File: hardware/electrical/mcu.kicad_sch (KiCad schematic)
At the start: 0 parts

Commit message: Add microcontroller and pinout to schematic
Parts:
- added C? (x2): 2u2, symbol Device:C_Small
- added C? (x14): 100n, symbol Device:C_Small
- added C?: 4u7, symbol Device:C_Small
- added C? (x2): 1u, symbol Device:C_Small
- added U?: STM32F446ZETx, Package_QFP:LQFP-144_20x20mm_P0.5mm, symbol MCU_ST_STM32F4:STM32F446ZETx
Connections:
- new net: C?.1, U?.71 (VCAP_1)
- new net: C?.1, U?.106 (VCAP_2)
- new net +3V3: C?.1, C?.1, C?.1, C?.1, C?.1, C?.1, C?.1, C?.1, C?.1, C?.1, C?.1, C?.1, C?.1, C?.1, C?.1, C?.1, C?.1, U?.108 (VDD), U?.121 (VDD), U?.131 (VDD), U?.144 (VDD), U?.17 (VDD), U?.30 (VDD), U?.32 (VREF+), U?.33 (VDDA), U?.39 (VDD), U?.52 (VDD), U?.62 (VDD), U?.72 (VDD), U?.84 (VDD), U?.95 (VDDUSB)
- new net BOOT0: U?.138 (BOOT0)
- new net DCMI_D0: U?.96 (PC6)
- new net DCMI_D1: U?.97 (PC7)
- new net DCMI_D2: U?.125 (PG10)
- new net DCMI_D3: U?.126 (PG11)
- new net DCMI_D5: U?.117 (PD3), U?.3 (PE4)
- new net DCMI_D6: U?.4 (PE5)
- new net DCMI_D7: U?.5 (PE6)
- new net DCMI_HSYNC: U?.40 (PA4)
- new net DCMI_PIXCLK: U?.42 (PA6)
- new net DCMI_VSYNC: U?.124 (PG9)
- new net FMC_A0: U?.10 (PF0)
- new net FMC_A1: U?.11 (PF1)
- new net FMC_A10: U?.56 (PG0)
- new net FMC_A11: U?.57 (PG1)
- new net FMC_A2: U?.12 (PF2)
- new net FMC_A3: U?.13 (PF3)
- new net FMC_A4: U?.14 (PF4)
- new net FMC_A5: U?.15 (PF5)
- new net FMC_A6: U?.50 (PF12)
- new net FMC_A7: U?.53 (PF13)
- new net FMC_A8: U?.54 (PF14)
- new net FMC_A9: U?.55 (PF15)
- new net FMC_BA0: U?.89 (PG4)
- new net FMC_BA1: U?.90 (PG5)
- new net FMC_D0: U?.85 (PD14)
- new net FMC_D1: U?.86 (PD15)
- new net FMC_D10: U?.66 (PE13)
- new net FMC_D11: U?.67 (PE14)
- new net FMC_D12: U?.68 (PE15)
- new net FMC_D13: U?.77 (PD8)
- new net FMC_D14: U?.78 (PD9)
- new net FMC_D15: U?.79 (PD10)
- new net FMC_D2: U?.114 (PD0)
- new net FMC_D3: U?.115 (PD1)
- new net FMC_D4: U?.58 (PE7)
- new net FMC_D5: U?.59 (PE8)
- new net FMC_D6: U?.60 (PE9)
- new net FMC_D7: U?.63 (PE10)
- new net FMC_D8: U?.64 (PE11)
- new net FMC_D9: U?.65 (PE12)
- new net FMC_NBL0: U?.141 (PE0)
- new net FMC_NBL1: U?.142 (PE1)
- new net FMC_SDCKE0: U?.45 (PC5)
- new net FMC_SDCLK: U?.93 (PG8)
- new net FMC_SDNCAS: U?.132 (PG15)
- new net FMC_SDNE0: U?.44 (PC4)
- new net FMC_SDNRAS: U?.49 (PF11)
- new net FMC_SDNWE: U?.43 (PA7)
- new net GND: C?.2, C?.2, C?.2, C?.2, C?.2, C?.2, C?.2, C?.2, C?.2, C?.2, C?.2, C?.2, C?.2, C?.2, C?.2, C?.2, C?.2, C?.2, C?.2, U?.107 (VSS), U?.120 (VSS), U?.130 (VSS), U?.16 (VSS), U?.31 (VSSA), U?.38 (VSS), U?.51 (VSS), U?.61 (VSS), U?.83 (VSS), U?.94 (VSS)
- new net I2C_SCL: U?.136 (PB6)
- new net I2C_SDA: U?.137 (PB7)
- new net NRST: U?.25 (NRST)
- new net PDR_ON: U?.143 (PDR_ON)
- new net RCC_OSC_IN: U?.23 (PH0)
- new net RCC_OSC_OUT: U?.24 (PH1)
- new net SDIO_CK: U?.113 (PC12)
- new net SDIO_CMD: U?.116 (PD2)
- new net SDIO_D0: U?.98 (PC8)
- new net SDIO_D1: U?.99 (PC9)
- new net SDIO_D2: U?.111 (PC10)
- new net SDIO_D3: U?.112 (PC11)
- new net SYS_JTCK-SWCLK: U?.109 (PA14)
- new net SYS_JTDO-SW0: U?.133 (PB3)
- new net SYS_JTMS-SWDIO: U?.105 (PA13)
- new net USB_OTG_HS_ULPI_CLK: U?.41 (PA5)
- new net USB_OTG_HS_ULPI_D0: U?.37 (PA3)
- new net USB_OTG_HS_ULPI_D1: U?.46 (PB0)
- new net USB_OTG_HS_ULPI_D2: U?.47 (PB1)
- new net USB_OTG_HS_ULPI_D3: U?.69 (PB10)
- new net USB_OTG_HS_ULPI_D4: U?.48 (PB2)
- new net USB_OTG_HS_ULPI_D5: U?.73 (PB12)
- new net USB_OTG_HS_ULPI_D6: U?.74 (PB13)
- new net USB_OTG_HS_ULPI_D7: U?.135 (PB5)
- new net USB_OTG_HS_ULPI_DIR: U?.28 (PC2)
- new net USB_OTG_HS_ULPI_NXT: U?.29 (PC3)
- new net USB_OTG_HS_ULPI_STP: U?.26 (PC0)
- no-connect marks 0 -> 41

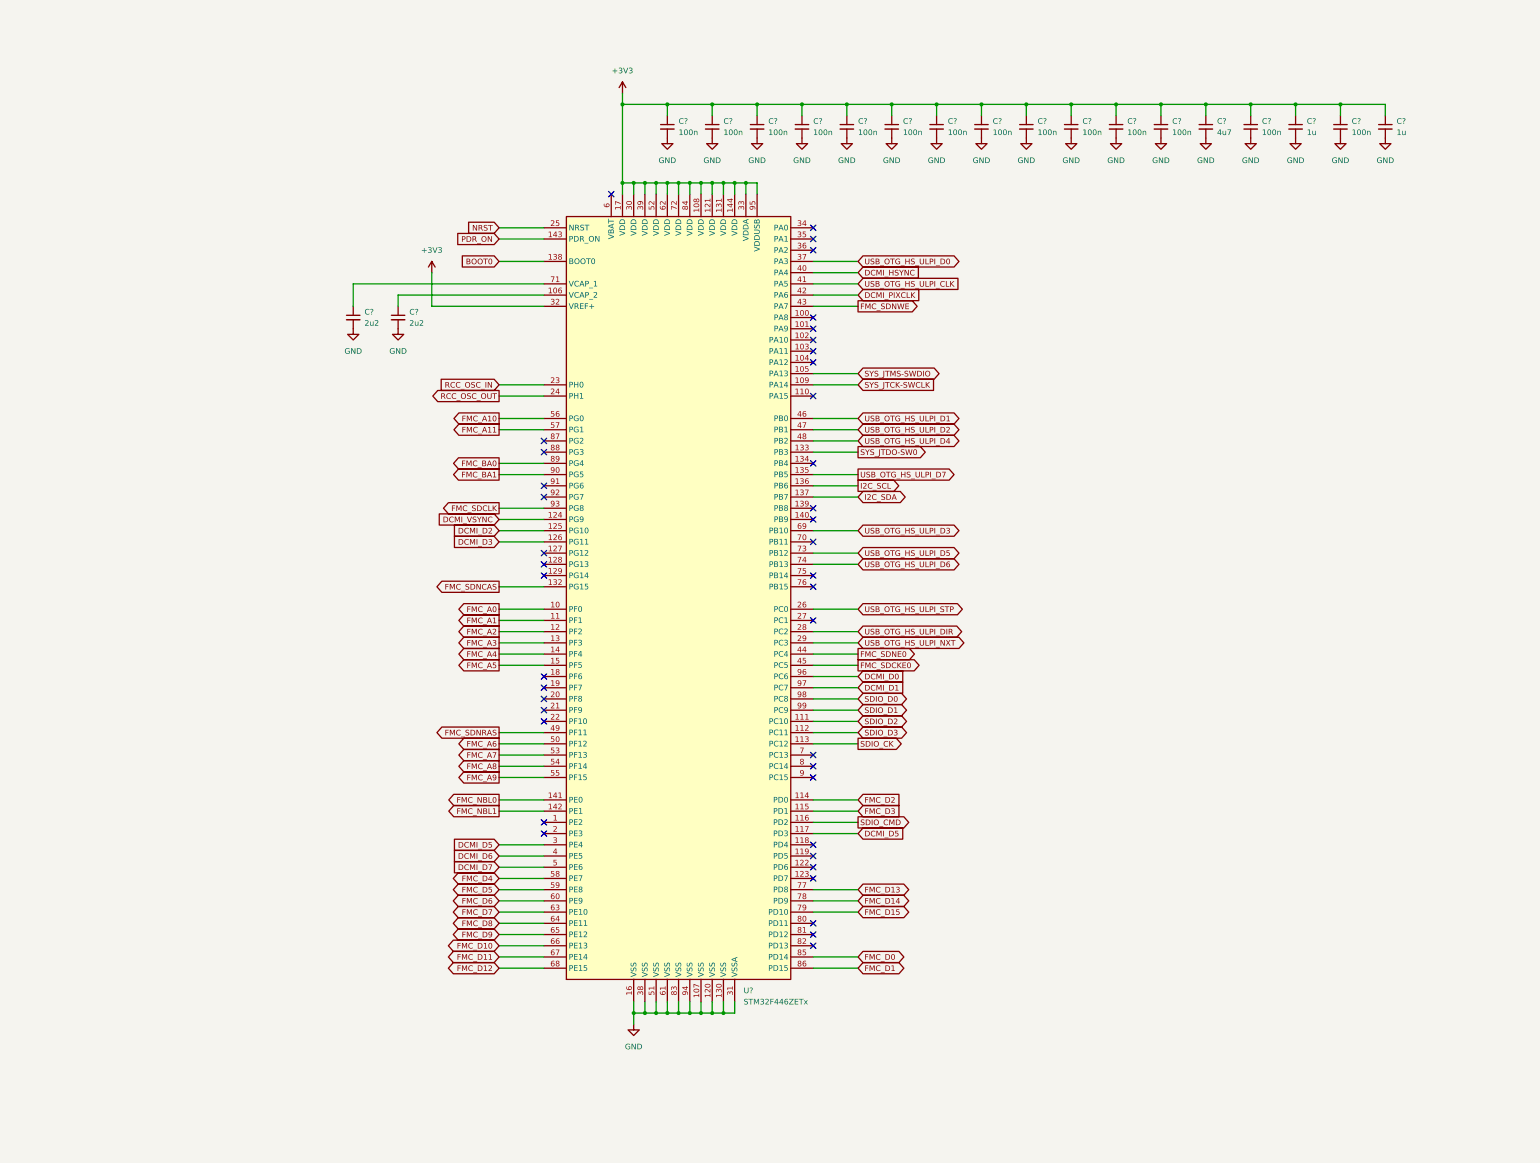
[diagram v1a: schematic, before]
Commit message: Add HSE oscillator circuit
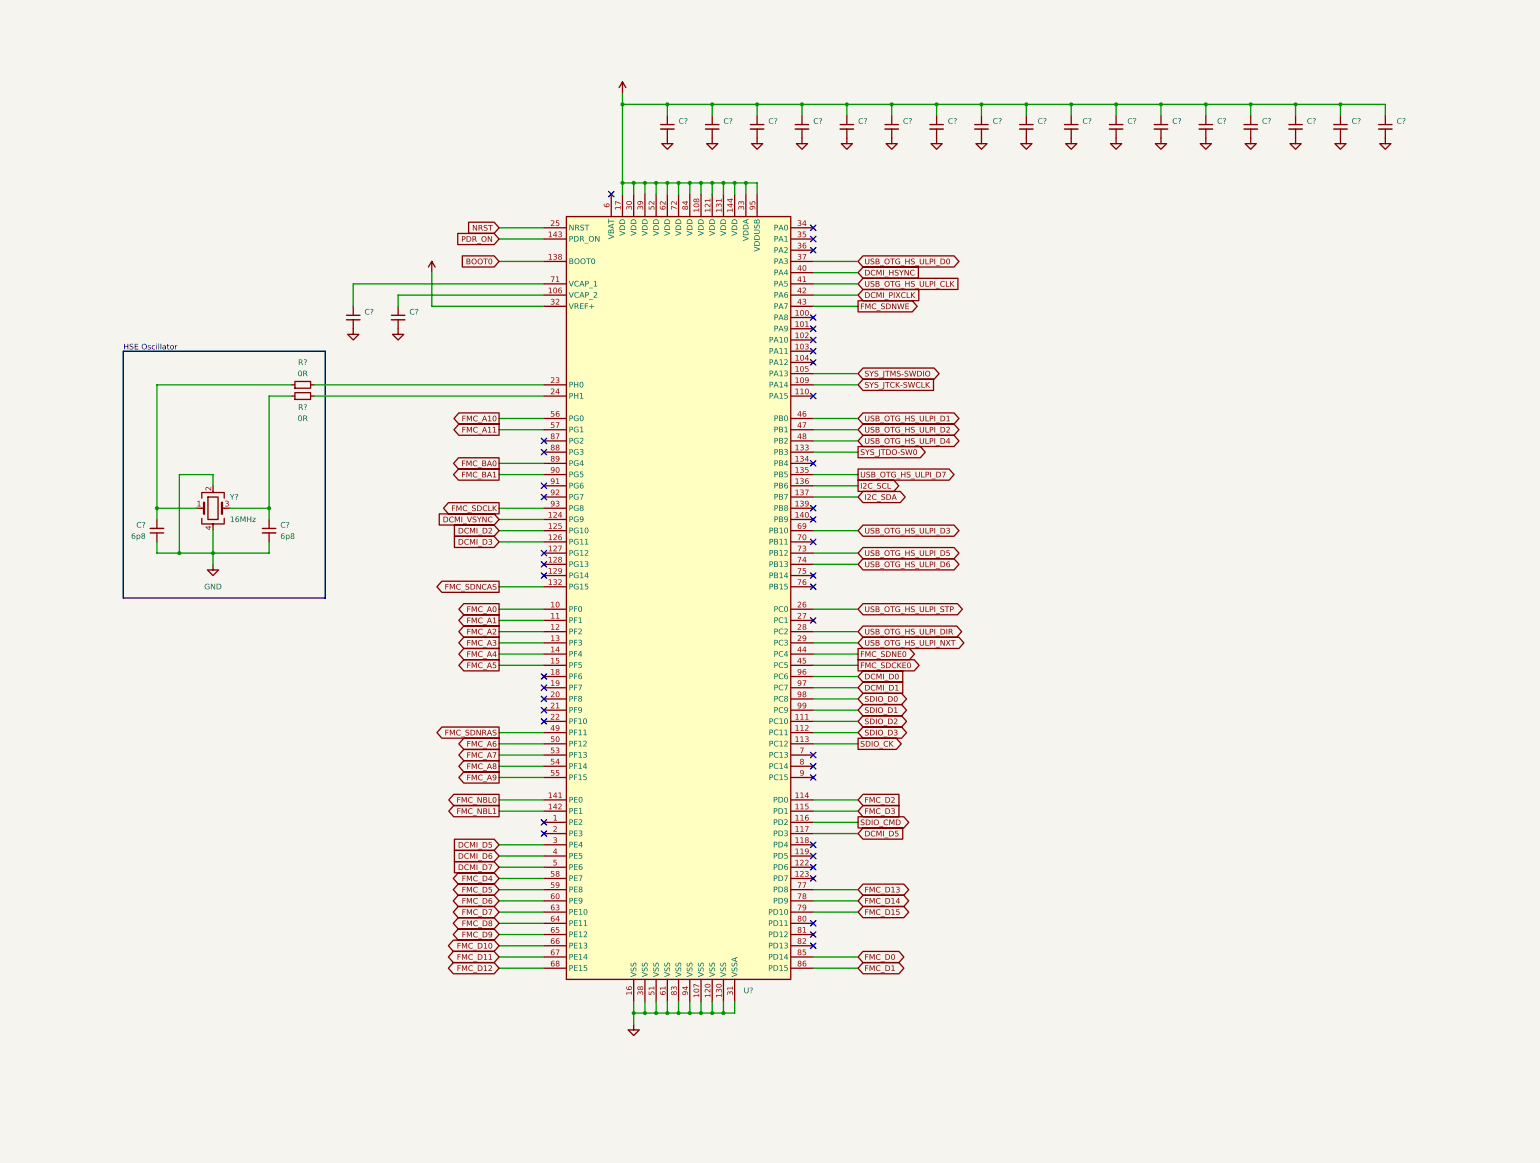
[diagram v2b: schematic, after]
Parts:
- added C? (x2): 6p8, symbol Device:C_Small
- added R? (x2): 0R, symbol Device:R_Small
- added Y?: 16MHz, symbol Device:Crystal_GND24
- C? (x2): value 2u2 -> (none)
- C? (x14): value 100n -> (none)
- C?: value 4u7 -> (none)
- C? (x2): value 1u -> (none)
- U?: value STM32F446ZETx -> (none); footprint Package_QFP:LQFP-144_20x20mm_P0.5mm -> (none)
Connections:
- net GND: now also C?.1, C?.2, Y?.2, Y?.4
- net RCC_OSC_IN: no longer names the net of U?.23 (PH0)
- net RCC_OSC_IN: now also R?.2
- net RCC_OSC_OUT: no longer names the net of U?.24 (PH1)
- net RCC_OSC_OUT: now also R?.2
- new net: C?.2, R?.1, Y?.1
- new net: C?.1, R?.1, Y?.3
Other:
- note added: "HSE Oscillator"

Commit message: Add serial wire debug connection and boot selection circuitry to schematic
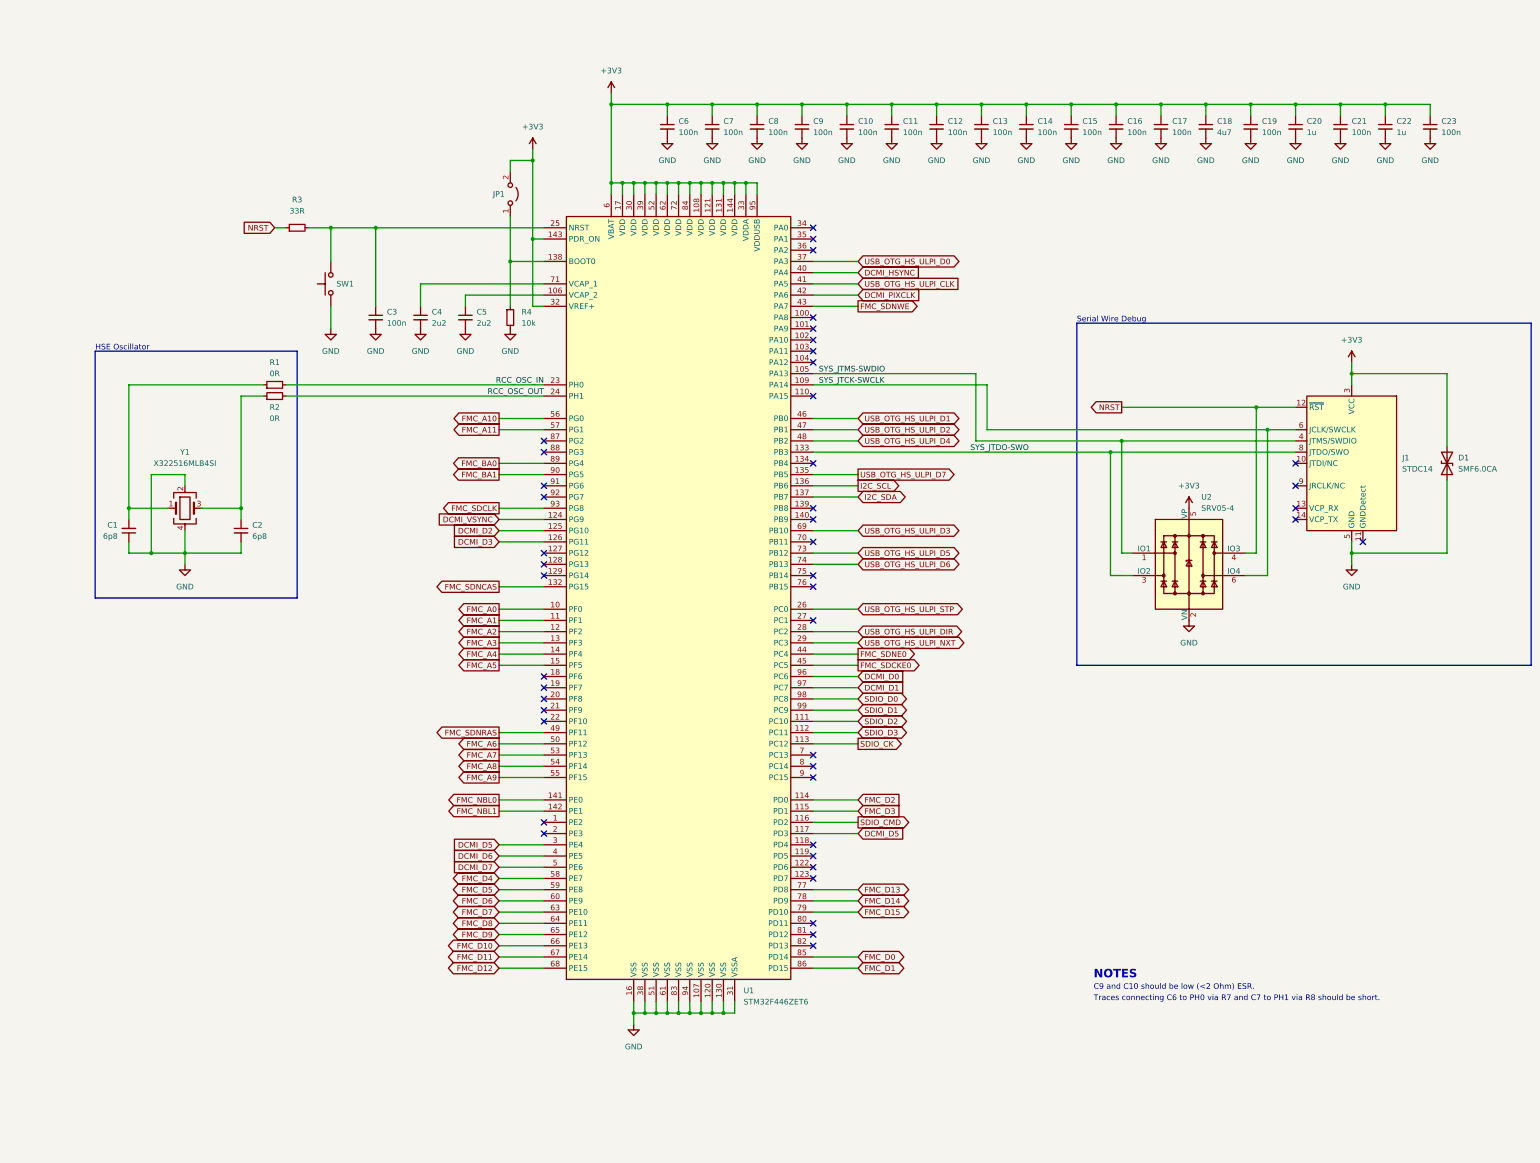
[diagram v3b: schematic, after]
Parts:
- added C23, C3: 100n, symbol Device:C_Small
- added D1: SMF6.0CA, symbol Device:D_TVS
- added J1: STDC14, symbol Connector:Conn_ST_STDC14
- added JP1: Jumper_2_Open, symbol Jumper:Jumper_2_Open
- added R3: 33R, symbol Device:R_Small
- added R4: 10k, symbol Device:R_Small
- added SW1: SW_Push, symbol Switch:SW_Push
- added U2: SRV05-4, Package_TO_SOT_SMD:SOT-23-6, symbol Power_Protection:SRV05-4
- C10, C11, C12, C13, C14, C15, C16, C17, C19, C21, C6, C7, C8, C9: renamed from C?; value (none) -> 100n
- C18: renamed from C?; value (none) -> 4u7
- C20, C22: renamed from C?; value (none) -> 1u
- C4, C5: renamed from C?; value (none) -> 2u2
- U1: renamed from U?; value (none) -> STM32F446ZET6; footprint (none) -> Package_QFP:LQFP-144_20x20mm_P0.5mm
- Y1: renamed from Y?; value 16MHz -> X322516MLB4SI
- gave numbers to parts that had none: 4
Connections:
- net PDR_ON is gone; now on net +3V3: U1.143 (PDR_ON)
- net +3V3: now also U1.6 (VBAT), C23.1, D1.2 (A2), J1.3 (VCC), JP1.2 (B), U2.5 (VP)
- net GND: now also C23.2, C3.2, D1.1 (A1), J1.5 (GND), J1.7 (GND), R4.2, SW1.1, U2.2 (VN)
- net NRST: now also J1.12 (~{RST}), R3.1, U2.4 (IO3); no longer U1.25 (NRST)
- net SYS_JTCK-SWCLK: now also J1.6 (JCLK/SWCLK), U2.6 (IO4)
- net SYS_JTMS-SWDIO: now also J1.4 (JTMS/SWDIO), U2.1 (IO1)
- net RCC_OSC_IN: now reaches R1.2, U1.23 (PH0)
- net RCC_OSC_OUT: now reaches R2.2, U1.24 (PH1)
- net BOOT0: no longer names the net of U1.138 (BOOT0)
- net BOOT0: now also JP1.1 (A), R4.1
- net SYS_JTDO-SW0 renamed SYS_JTDO-SWO
- net SYS_JTDO-SWO: now also J1.8 (JTDO/SWO), U2.3 (IO2)
- new net: C3.1, R3.2, SW1.2, U1.25 (NRST)
- no-connect marks 41 -> 45
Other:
- note added: "C9 and C10 should be low (<2 Ohm) ESR."
- note added: "NOTES"
- note added: "Serial Wire Debug"
- note added: "Traces connecting C6 to PH0 via R7 and C7 to PH1 via R8 should be short."
- moved on the sheet: C1, C2, C4, C5, R1, R2, Y1

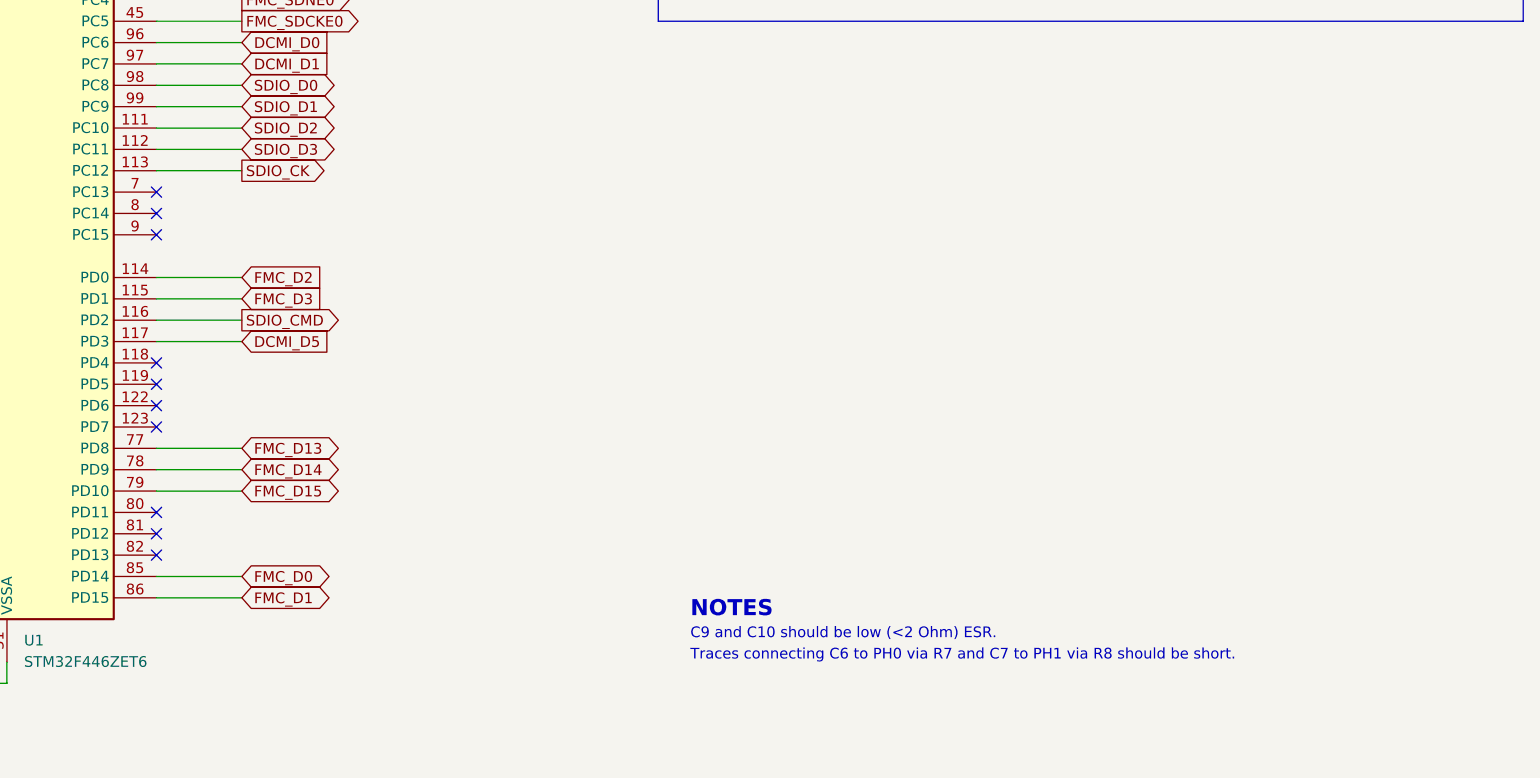
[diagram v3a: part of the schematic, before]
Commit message: Add status LED, power switch and charge detction
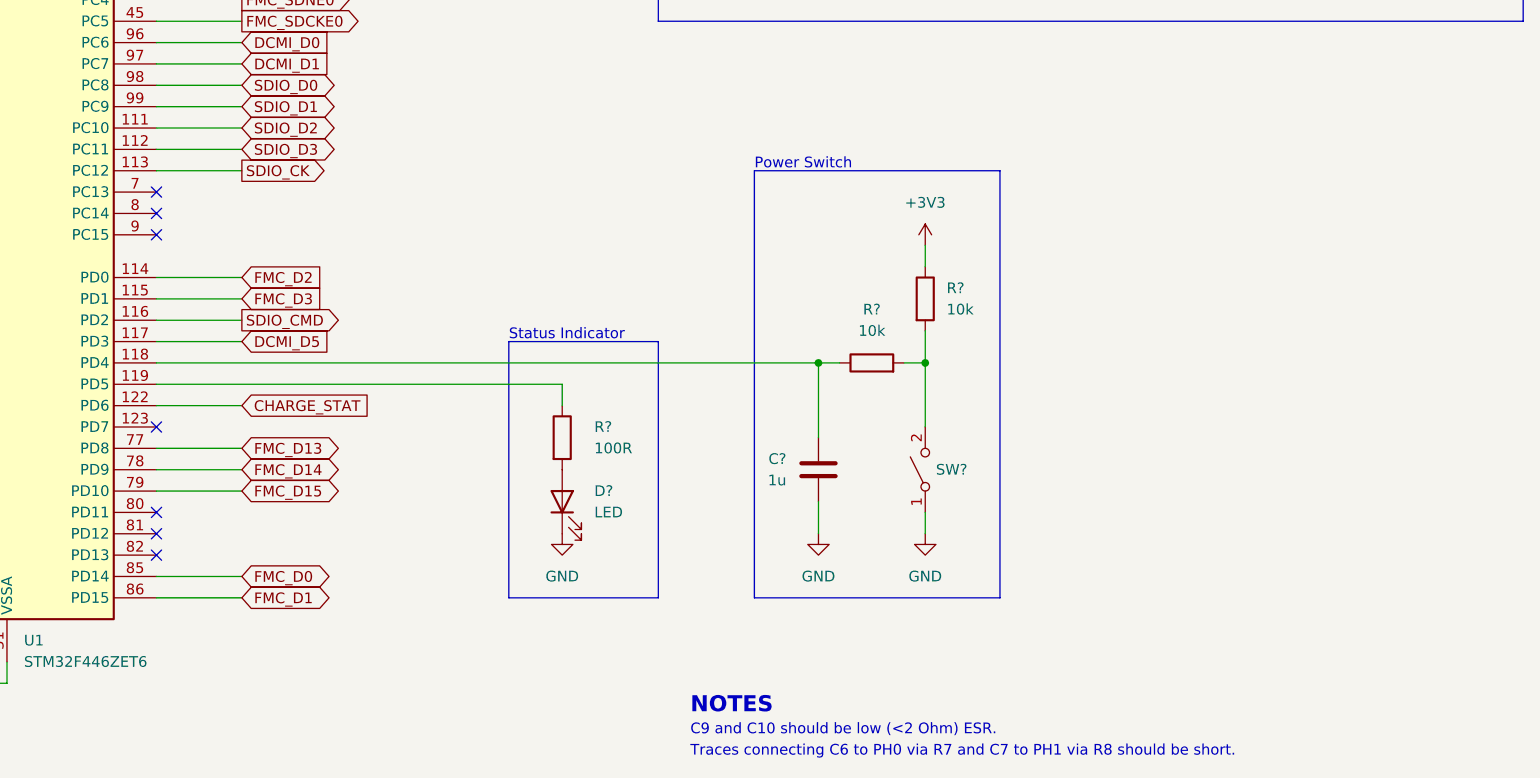
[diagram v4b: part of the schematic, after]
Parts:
- added C?: 1u, symbol Device:C
- added D?: LED, symbol Device:LED
- added R? (x2): 10k, symbol Device:R
- added R?: 100R, symbol Device:R
- added SW?: SW_SPST, symbol Switch:SW_SPST
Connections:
- net +3V3: now also R?.1
- net GND: now also C?.1, D?.1 (K), SW?.1 (A)
- net at U1.118 (PD4): now also C?.2, R?.1
- net at U1.119 (PD5): now also R?.1
- net CHARGE_STAT: now reaches U1.122 (PD6)
- new net: R?.2, R?.2, SW?.2 (B)
- new net: D?.2 (A), R?.2
- no-connect marks 45 -> 42
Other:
- note added: "Power Switch"
- note added: "Status Indicator"
